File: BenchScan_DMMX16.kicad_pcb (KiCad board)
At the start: 4 copper layers, 220 x 110 mm, 0 parts

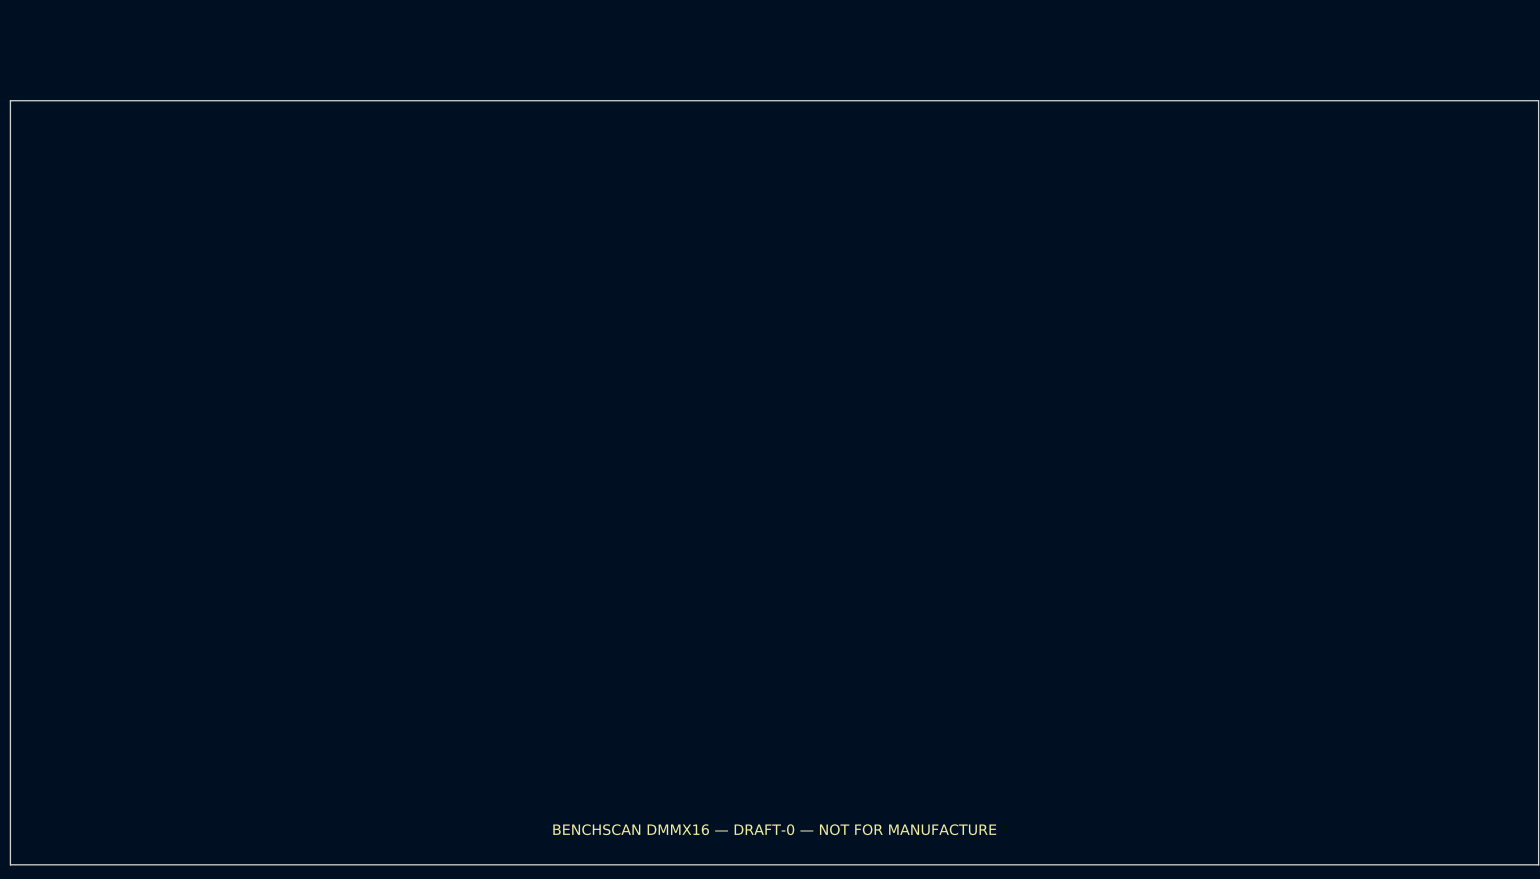
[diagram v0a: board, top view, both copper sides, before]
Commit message: Prepare four-layer PCB for component placement
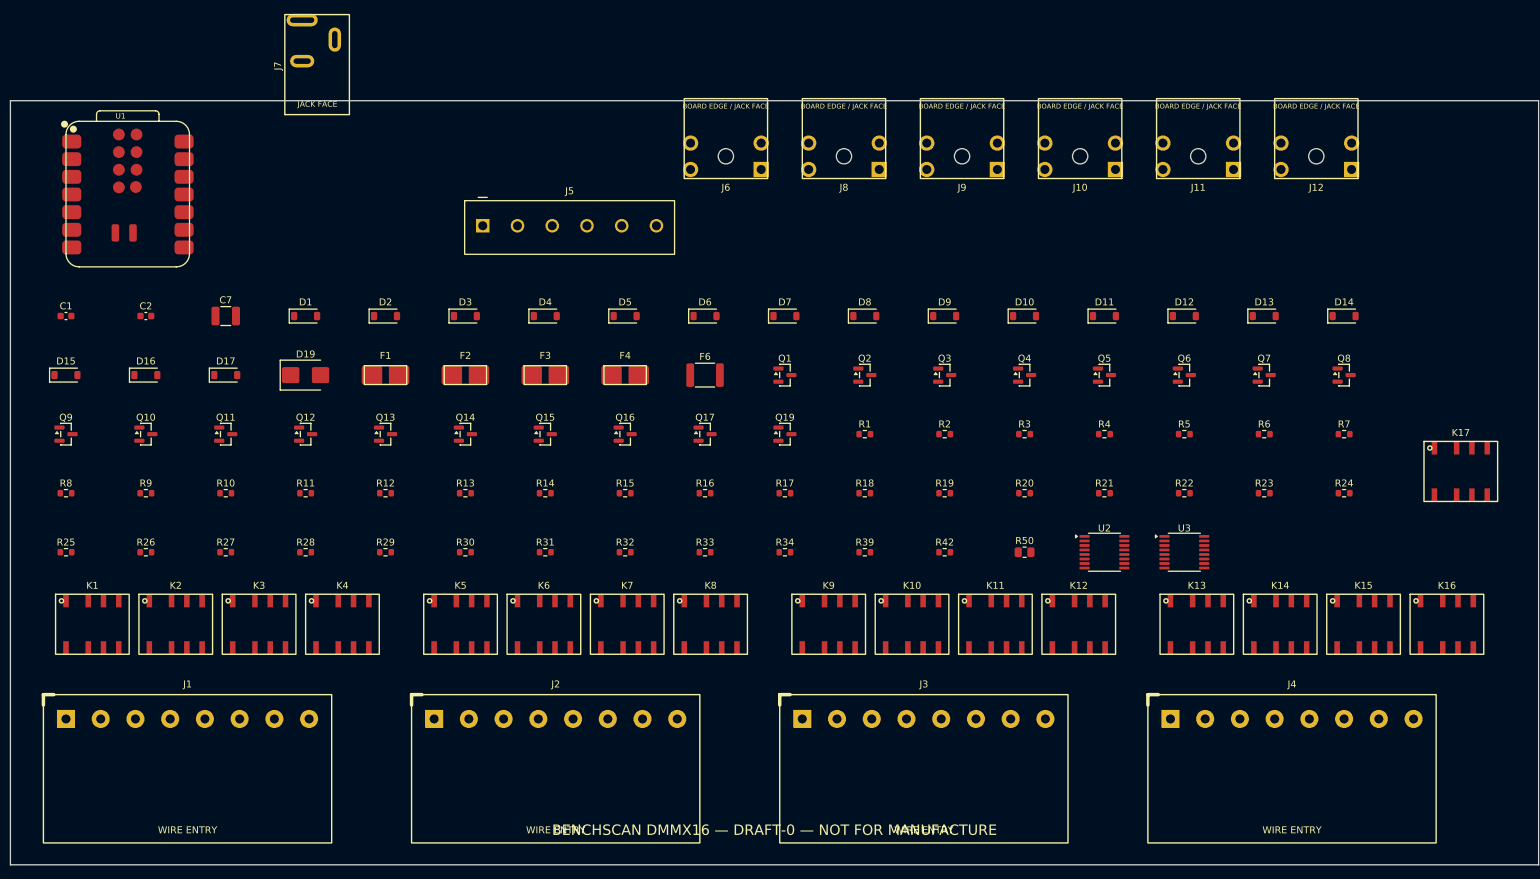
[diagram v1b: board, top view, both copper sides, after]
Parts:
- added C1: 100nF, C_0603_1608Metric, F.Cu at (8.00, 31.0)
- added C2: 100nF, C_0603_1608Metric, F.Cu at (19.5, 31.0)
- added C7: 47uF 10V, C_1210_3225Metric, F.Cu at (31.0, 31.0)
- added D1: 1N4148W, D_SOD-123, F.Cu at (42.5, 31.0)
- added D10: 1N4148W, D_SOD-123, F.Cu at (146.0, 31.0)
- added D11: 1N4148W, D_SOD-123, F.Cu at (157.5, 31.0)
- added D12: 1N4148W, D_SOD-123, F.Cu at (169.0, 31.0)
- added D13: 1N4148W, D_SOD-123, F.Cu at (180.5, 31.0)
- added D14: 1N4148W, D_SOD-123, F.Cu at (192.0, 31.0)
- added D15: 1N4148W, D_SOD-123, F.Cu at (8.00, 39.5)
- added D16: 1N4148W, D_SOD-123, F.Cu at (19.5, 39.5)
- added D17: 1N4148W, D_SOD-123, F.Cu at (31.0, 39.5)
- added D19: SMBJ5.0A, D_SMB, F.Cu at (42.5, 39.5)
- added D2: 1N4148W, D_SOD-123, F.Cu at (54.0, 31.0)
- added D3: 1N4148W, D_SOD-123, F.Cu at (65.5, 31.0)
- added D4: 1N4148W, D_SOD-123, F.Cu at (77.0, 31.0)
- added D5: 1N4148W, D_SOD-123, F.Cu at (88.5, 31.0)
- added D6: 1N4148W, D_SOD-123, F.Cu at (100.0, 31.0)
- added D7: 1N4148W, D_SOD-123, F.Cu at (111.5, 31.0)
- added D8: 1N4148W, D_SOD-123, F.Cu at (123.0, 31.0)
- added D9: 1N4148W, D_SOD-123, F.Cu at (134.5, 31.0)
- added F1: 0451.500MRL 500mA, Fuse_Littelfuse_0451_NANO2_2410, F.Cu at (54.0, 39.5)
- added F2: 0451.500MRL 500mA, Fuse_Littelfuse_0451_NANO2_2410, F.Cu at (65.5, 39.5)
- added F3: 0451.500MRL 500mA, Fuse_Littelfuse_0451_NANO2_2410, F.Cu at (77.0, 39.5)
- added F4: 0451.500MRL 500mA, Fuse_Littelfuse_0451_NANO2_2410, F.Cu at (88.5, 39.5)
- added F6: 1812L150/12DR, Fuse_1812_4532Metric, F.Cu at (100.0, 39.5)
- added J1: Phoenix 1190370 8POS, Phoenix_1190370_LPTA-2.5-8-5.0, F.Cu at (8.00, 89.0)
- added J10: POMONA 73099 BLACK, Pomona_73099_RightAngle_SafetyJack, F.Cu at (154.0, 8.00)
- added J11: POMONA 73099 RED, Pomona_73099_RightAngle_SafetyJack, F.Cu at (171.0, 8.00)
- added J12: POMONA 73099 BLACK, Pomona_73099_RightAngle_SafetyJack, F.Cu at (188.0, 8.00)
- added J2: Phoenix 1190370 8POS, Phoenix_1190370_LPTA-2.5-8-5.0, F.Cu at (61.0, 89.0)
- added J3: Phoenix 1190370 8POS, Phoenix_1190370_LPTA-2.5-8-5.0, F.Cu at (114.0, 89.0)
- added J4: Phoenix 1190370 8POS, Phoenix_1190370_LPTA-2.5-8-5.0, F.Cu at (167.0, 89.0)
- added J5: 691137710006 DMM, J_Wurth_WR-TBL_691137710006, F.Cu at (68.0, 18.0)
- added J6: POMONA 73099 RED, Pomona_73099_RightAngle_SafetyJack, F.Cu at (103.0, 8.00)
- added J7: 54-00129 BARREL 5V, Tensility_54-00129_DCJack, F.Cu at (42.0, 2.00)
- added J8: POMONA 73099 BLACK, Pomona_73099_RightAngle_SafetyJack, F.Cu at (120.0, 8.00)
- added J9: POMONA 73099 RED, Pomona_73099_RightAngle_SafetyJack, F.Cu at (137.0, 8.00)
- added K1: UD2-5NE, Relay_KEMET_UD2_NE, F.Cu at (8.00, 72.0)
- added K10: UD2-5NE, Relay_KEMET_UD2_NE, F.Cu at (126.0, 72.0)
- added K11: UD2-5NE, Relay_KEMET_UD2_NE, F.Cu at (138.0, 72.0)
- added K12: UD2-5NE, Relay_KEMET_UD2_NE, F.Cu at (150.0, 72.0)
- added K13: UD2-5NE, Relay_KEMET_UD2_NE, F.Cu at (167.0, 72.0)
- added K14: UD2-5NE, Relay_KEMET_UD2_NE, F.Cu at (179.0, 72.0)
- added K15: UD2-5NE, Relay_KEMET_UD2_NE, F.Cu at (191.0, 72.0)
- added K16: UD2-5NE, Relay_KEMET_UD2_NE, F.Cu at (203.0, 72.0)
- added K17: UD2-5NE, Relay_KEMET_UD2_NE, F.Cu at (205.0, 50.0)
- added K2: UD2-5NE, Relay_KEMET_UD2_NE, F.Cu at (20.0, 72.0)
- added K3: UD2-5NE, Relay_KEMET_UD2_NE, F.Cu at (32.0, 72.0)
- added K4: UD2-5NE, Relay_KEMET_UD2_NE, F.Cu at (44.0, 72.0)
- added K5: UD2-5NE, Relay_KEMET_UD2_NE, F.Cu at (61.0, 72.0)
- added K6: UD2-5NE, Relay_KEMET_UD2_NE, F.Cu at (73.0, 72.0)
- added K7: UD2-5NE, Relay_KEMET_UD2_NE, F.Cu at (85.0, 72.0)
- added K8: UD2-5NE, Relay_KEMET_UD2_NE, F.Cu at (97.0, 72.0)
- added K9: UD2-5NE, Relay_KEMET_UD2_NE, F.Cu at (114.0, 72.0)
- added Q1: 2N7002K, SOT-23, F.Cu at (111.5, 39.5)
- added Q10: 2N7002K, SOT-23, F.Cu at (19.5, 48.0)
- added Q11: 2N7002K, SOT-23, F.Cu at (31.0, 48.0)
- added Q12: 2N7002K, SOT-23, F.Cu at (42.5, 48.0)
- added Q13: 2N7002K, SOT-23, F.Cu at (54.0, 48.0)
- added Q14: 2N7002K, SOT-23, F.Cu at (65.5, 48.0)
- added Q15: 2N7002K, SOT-23, F.Cu at (77.0, 48.0)
- added Q16: 2N7002K, SOT-23, F.Cu at (88.5, 48.0)
- added Q17: 2N7002K, SOT-23, F.Cu at (100.0, 48.0)
- added Q19: AO3401A, SOT-23, F.Cu at (111.5, 48.0)
- added Q2: 2N7002K, SOT-23, F.Cu at (123.0, 39.5)
- added Q3: 2N7002K, SOT-23, F.Cu at (134.5, 39.5)
- added Q4: 2N7002K, SOT-23, F.Cu at (146.0, 39.5)
- added Q5: 2N7002K, SOT-23, F.Cu at (157.5, 39.5)
- added Q6: 2N7002K, SOT-23, F.Cu at (169.0, 39.5)
- added Q7: 2N7002K, SOT-23, F.Cu at (180.5, 39.5)
- added Q8: 2N7002K, SOT-23, F.Cu at (192.0, 39.5)
- added Q9: 2N7002K, SOT-23, F.Cu at (8.00, 48.0)
- added R1: 100R, R_0603_1608Metric, F.Cu at (123.0, 48.0)
- added R10: 100R, R_0603_1608Metric, F.Cu at (31.0, 56.5)
- added R11: 100R, R_0603_1608Metric, F.Cu at (42.5, 56.5)
- added R12: 100R, R_0603_1608Metric, F.Cu at (54.0, 56.5)
- added R13: 100R, R_0603_1608Metric, F.Cu at (65.5, 56.5)
- added R14: 100R, R_0603_1608Metric, F.Cu at (77.0, 56.5)
- added R15: 100R, R_0603_1608Metric, F.Cu at (88.5, 56.5)
- added R16: 100R, R_0603_1608Metric, F.Cu at (100.0, 56.5)
- added R17: 100R, R_0603_1608Metric, F.Cu at (111.5, 56.5)
- added R18: 47k, R_0603_1608Metric, F.Cu at (123.0, 56.5)
- added R19: 47k, R_0603_1608Metric, F.Cu at (134.5, 56.5)
- added R2: 100R, R_0603_1608Metric, F.Cu at (134.5, 48.0)
- added R20: 47k, R_0603_1608Metric, F.Cu at (146.0, 56.5)
- added R21: 47k, R_0603_1608Metric, F.Cu at (157.5, 56.5)
- added R22: 47k, R_0603_1608Metric, F.Cu at (169.0, 56.5)
- added R23: 47k, R_0603_1608Metric, F.Cu at (180.5, 56.5)
- added R24: 47k, R_0603_1608Metric, F.Cu at (192.0, 56.5)
- added R25: 47k, R_0603_1608Metric, F.Cu at (8.00, 65.0)
- added R26: 47k, R_0603_1608Metric, F.Cu at (19.5, 65.0)
- added R27: 47k, R_0603_1608Metric, F.Cu at (31.0, 65.0)
- added R28: 47k, R_0603_1608Metric, F.Cu at (42.5, 65.0)
- added R29: 47k, R_0603_1608Metric, F.Cu at (54.0, 65.0)
- added R3: 100R, R_0603_1608Metric, F.Cu at (146.0, 48.0)
- added R30: 47k, R_0603_1608Metric, F.Cu at (65.5, 65.0)
- added R31: 47k, R_0603_1608Metric, F.Cu at (77.0, 65.0)
- added R32: 47k, R_0603_1608Metric, F.Cu at (88.5, 65.0)
- added R33: 47k, R_0603_1608Metric, F.Cu at (100.0, 65.0)
- added R34: 47k, R_0603_1608Metric, F.Cu at (111.5, 65.0)
- added R39: 10k, R_0603_1608Metric, F.Cu at (123.0, 65.0)
- added R4: 100R, R_0603_1608Metric, F.Cu at (157.5, 48.0)
- added R42: 100k, R_0603_1608Metric, F.Cu at (134.5, 65.0)
- added R5: 100R, R_0603_1608Metric, F.Cu at (169.0, 48.0)
- added R50: 0R LINK, R_0805_2012Metric, F.Cu at (146.0, 65.0)
- added R6: 100R, R_0603_1608Metric, F.Cu at (180.5, 48.0)
- added R7: 100R, R_0603_1608Metric, F.Cu at (192.0, 48.0)
- added R8: 100R, R_0603_1608Metric, F.Cu at (8.00, 56.5)
- added R9: 100R, R_0603_1608Metric, F.Cu at (19.5, 56.5)
- added U1: XIAO ESP32-C6 / 113991254, XIAO-ESP32-C6-SMD, F.Cu at (8.00, 24.0)
- added U2: SN74HC595PWR, TSSOP-16_4.4x5mm_P0.65mm, F.Cu at (157.5, 65.0)
- added U3: SN74HC595PWR, TSSOP-16_4.4x5mm_P0.65mm, F.Cu at (169.0, 65.0)

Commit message: Update preliminary component placement
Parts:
- moved J7 53.7 mm to (85.7, 33.3), turned to -90 degrees
- moved C1 51.2 mm to (48.0, 63.0)
- moved C2 51.2 mm to (59.5, 63.0)
- moved C7 51.2 mm to (71.0, 63.0)
- moved D1 51.2 mm to (82.5, 63.0)
- moved D10 51.2 mm to (186.0, 63.0)
- moved D11 51.2 mm to (197.5, 63.0)
- moved D12 51.2 mm to (209.0, 63.0)
- moved D13 51.2 mm to (220.5, 63.0)
- moved D14 51.2 mm to (232.0, 63.0)
- moved D15 51.2 mm to (48.0, 71.5)
- moved D16 51.2 mm to (59.5, 71.5)
- moved D17 51.2 mm to (71.0, 71.5)
- moved D19 51.2 mm to (82.5, 71.5)
- moved D2 51.2 mm to (94.0, 63.0)
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
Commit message: Optimize relay driver placement
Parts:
- moved D16 180.3 mm to (238.0, 97.0)
- moved D15 179.8 mm to (226.0, 97.0)
- moved D17 167.1 mm to (238.0, 65.0)
- moved R1 117.1 mm to (46.5, 92.0)
- moved R2 116.6 mm to (58.5, 92.0)
- moved R3 116.1 mm to (70.5, 92.0)
- moved R4 115.6 mm to (82.5, 92.0)
- moved R18 113.1 mm to (50.0, 92.0)
- moved C2 112.6 mm to (170.5, 82.0)
- moved R19 112.6 mm to (62.0, 92.0)
- moved R20 112.1 mm to (74.0, 92.0)
- moved R21 111.6 mm to (86.0, 92.0)
- moved R5 111.1 mm to (98.5, 92.0)
- moved R6 110.7 mm to (110.5, 92.0)
- moved Q1 110.4 mm to (43.0, 92.0)
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
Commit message: Correct J1-J4 Phoenix terminal footprints
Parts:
- J1, J2, J3, J4: footprint Phoenix_1190370_LPTA-2.5-8-5.0 -> Phoenix_1190370_LPTA-2.5-8-5.0_16THT_Paired

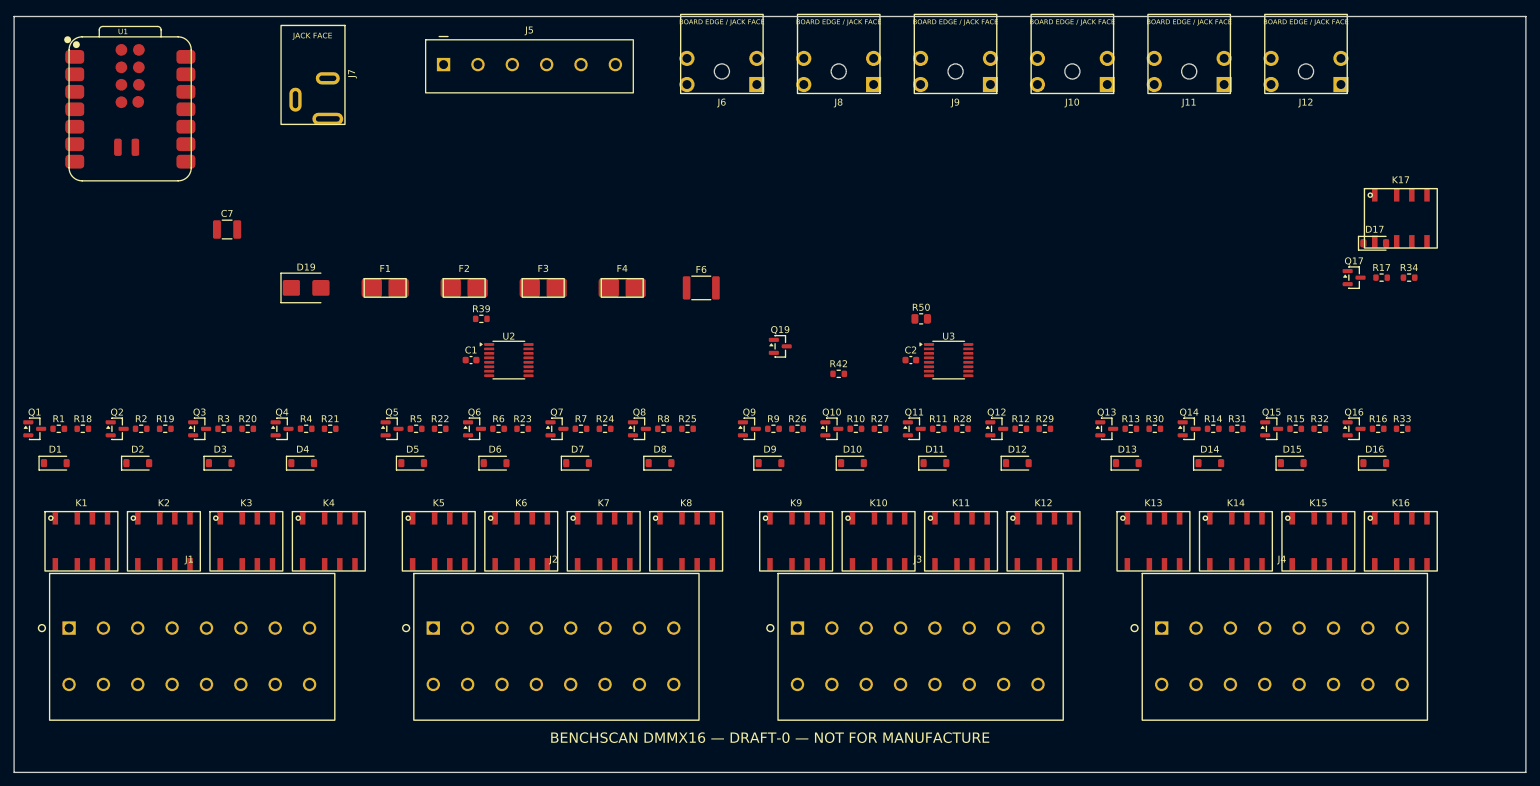
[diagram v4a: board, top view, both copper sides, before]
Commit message: Add corner mounting holes
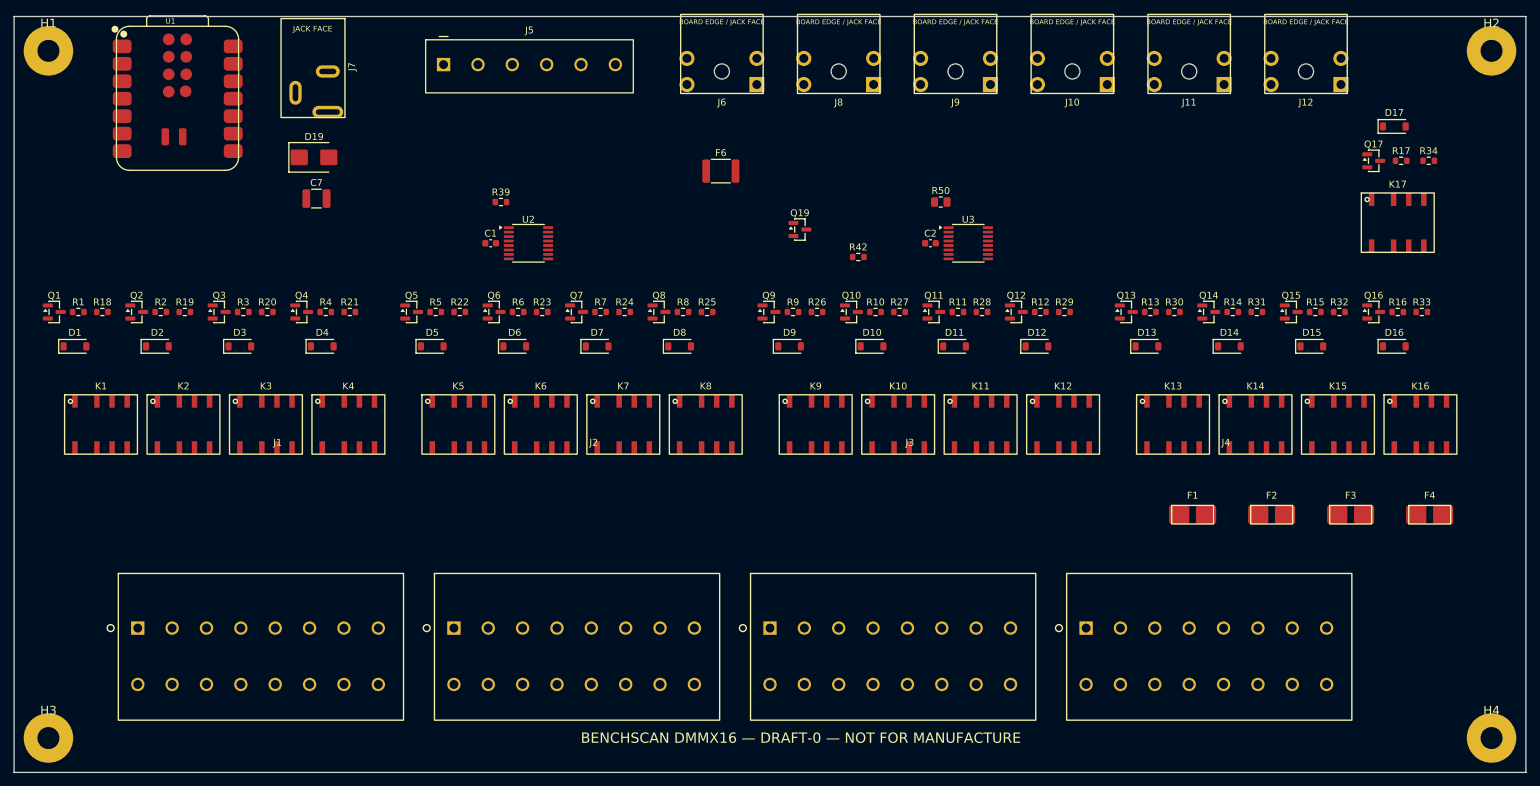
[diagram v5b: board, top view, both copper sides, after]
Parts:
- added H1: MountingHole_3.20mm, MountingHole_3.20mm, F.Cu at (45.0, 37.0)
- added H2: MountingHole_3.20mm, MountingHole_3.20mm, F.Cu at (255.0, 37.0)
- added H3: MountingHole_3.20mm, MountingHole_3.20mm, F.Cu at (45.0, 137.0)
- added H4: MountingHole_3.20mm, MountingHole_3.20mm, F.Cu at (255.0, 137.0)
- moved F1 122.0 mm to (211.5, 104.5)
- moved F2 122.0 mm to (223.0, 104.5)
- moved F3 122.0 mm to (234.5, 104.5)
- moved F4 122.0 mm to (246.0, 104.5)
- moved D19 19.0 mm to (83.7, 52.5)
- moved D1 17.2 mm to (48.9, 80.0)
- moved D2 17.2 mm to (60.9, 80.0)
- moved K1 17.2 mm to (48.9, 88.0)
- moved K2 17.2 mm to (60.9, 88.0)
- moved Q1 17.2 mm to (45.9, 75.0)
- moved Q2 17.2 mm to (57.9, 75.0)
- moved R1 17.2 mm to (49.4, 75.0)
- moved R18 17.2 mm to (52.9, 75.0)
- moved R2 17.2 mm to (61.4, 75.0)
- moved C1 17.2 mm to (109.3, 65.0)
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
